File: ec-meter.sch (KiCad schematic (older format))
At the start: 35 parts, among them P1 Probe, P2 V+, P3 OUT, P4 V-, U1 LM324, U2 LM324

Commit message: Started PCB, did some layout, fix some references
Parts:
- C1, C2, C3: footprint visgence_parts:SM1206POL_VIS -> visgence_parts:SM0603_VIS
- C5: footprint (none) -> visgence_parts:SM1206POL_VIS
- D1, D2: footprint (none) -> visgence_parts:SOD-323
- D3, D4: footprint (none) -> LEDs:LED_0603
- P1, P2, P3, P4: footprint (none) -> visgence_parts:Term3.5-2
- R1, R10, R11, R12, R2, R3, R4, R5, R6, R7, R8, R9: footprint visgence_parts:SM1206_VIS -> visgence_parts:SM0603_VIS
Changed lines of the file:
@@
 F 0 "R4" V 2880 1950 50  0000 C CNN
 F 1 "22k" V 2800 1950 50  0000 C CNN
-F 2 "visgence_parts:SM1206_VIS" V 2730 1950 50  0001 C CNN
+F 2 "visgence_parts:SM0603_VIS" V 2730 1950 50  0001 C CNN
 F 3 "" H 2800 1950 50  0000 C CNN
 	1    2800 1950
@@
 F 0 "R2" V 1680 2200 50  0000 C CNN
 F 1 "22k" V 1600 2200 50  0000 C CNN
-F 2 "visgence_parts:SM1206_VIS" V 1530 2200 50  0001 C CNN
+F 2 "visgence_parts:SM0603_VIS" V 1530 2200 50  0001 C CNN
 F 3 "" H 1600 2200 50  0000 C CNN
 	1    1600 2200
@@
 F 0 "R1" V 1430 2200 50  0000 C CNN
 F 1 "10k" V 1350 2200 50  0000 C CNN
-F 2 "visgence_parts:SM1206_VIS" V 1280 2200 50  0001 C CNN
+F 2 "visgence_parts:SM0603_VIS" V 1280 2200 50  0001 C CNN
 F 3 "" H 1350 2200 50  0000 C CNN
 	1    1350 2200
@@
 F 0 "C2" H 2025 2500 50  0000 L CNN
 F 1 "33nF" H 2025 2300 50  0000 L CNN
-F 2 "visgence_parts:SM1206POL_VIS" H 2038 2250 50  0001 C CNN
+F 2 "visgence_parts:SM0603_VIS" H 2038 2250 50  0001 C CNN
 F 3 "" H 2000 2400 50  0000 C CNN
 	1    2000 2400
@@
 F 0 "C1" H 1075 2000 50  0000 L CNN
 F 1 "33nF" H 1075 1800 50  0000 L CNN
-F 2 "visgence_parts:SM1206POL_VIS" H 1088 1750 50  0001 C CNN
+F 2 "visgence_parts:SM0603_VIS" H 1088 1750 50  0001 C CNN
 F 3 "" H 1050 1900 50  0000 C CNN
 	1    1050 1900
@@
 F 0 "R3" V 2880 1250 50  0000 C CNN
 F 1 "22k" V 2800 1250 50  0000 C CNN
-F 2 "visgence_parts:SM1206_VIS" V 2730 1250 50  0001 C CNN
+F 2 "visgence_parts:SM0603_VIS" V 2730 1250 50  0001 C CNN
 F 3 "" H 2800 1250 50  0000 C CNN
 	1    2800 1250
@@
 F 0 "C3" H 3525 2500 50  0000 L CNN
 F 1 "33nF" H 3525 2300 50  0000 L CNN
-F 2 "visgence_parts:SM1206POL_VIS" H 3538 2250 50  0001 C CNN
+F 2 "visgence_parts:SM0603_VIS" H 3538 2250 50  0001 C CNN
 F 3 "" H 3500 2400 50  0000 C CNN
 	1    3500 2400
@@
 F 0 "R8" V 4380 1850 50  0000 C CNN
 F 1 "100k" V 4300 1850 50  0000 C CNN
-F 2 "visgence_parts:SM1206_VIS" V 4230 1850 50  0001 C CNN
+F 2 "visgence_parts:SM0603_VIS" V 4230 1850 50  0001 C CNN
 F 3 "" H 4300 1850 50  0000 C CNN
 	1    4300 1850
@@
 F 0 "R9" V 4680 2150 50  0000 C CNN
 F 1 "3.3k" V 4600 2150 50  0000 C CNN
-F 2 "visgence_parts:SM1206_VIS" V 4530 2150 50  0001 C CNN
+F 2 "visgence_parts:SM0603_VIS" V 4530 2150 50  0001 C CNN
 F 3 "" H 4600 2150 50  0000 C CNN
 	1    4600 2150
@@
 F 0 "R10" V 5930 1700 50  0000 C CNN
 F 1 "4.7k" V 5850 1700 50  0000 C CNN
-F 2 "visgence_parts:SM1206_VIS" V 5780 1700 50  0001 C CNN
+F 2 "visgence_parts:SM0603_VIS" V 5780 1700 50  0001 C CNN
 F 3 "" H 5850 1700 50  0000 C CNN
 	1    5850 1700
@@
 F 0 "P1" H 7075 4925 50  0000 C CNN
 F 1 "Probe" V 7175 4775 50  0000 C CNN
-F 2 "" H 7075 4775 50  0001 C CNN
+F 2 "visgence_parts:Term3.5-2" H 7075 4775 50  0001 C CNN
 F 3 "" H 7075 4775 50  0000 C CNN
 	1    7075 4775
@@
 F 0 "D1" H 2750 5000 50  0000 C CNN
 F 1 "D" H 2750 4800 50  0000 C CNN
-F 2 "" H 2750 4900 50  0001 C CNN
+F 2 "visgence_parts:SOD-323" H 2750 4900 50  0001 C CNN
 F 3 "" H 2750 4900 50  0000 C CNN
 	1    2750 4900
@@
 F 0 "D2" H 3550 4550 50  0000 C CNN
 F 1 "D" H 3550 4350 50  0000 C CNN
-F 2 "" H 3550 4450 50  0001 C CNN
+F 2 "visgence_parts:SOD-323" H 3550 4450 50  0001 C CNN
 F 3 "" H 3550 4450 50  0000 C CNN
 	1    3550 4450
@@
 F 0 "R5" V 3630 4850 50  0000 C CNN
 F 1 "3.3K" V 3550 4850 50  0000 C CNN
-F 2 "visgence_parts:SM1206_VIS" V 3480 4850 50  0001 C CNN
+F 2 "visgence_parts:SM0603_VIS" V 3480 4850 50  0001 C CNN
 F 3 "" H 3550 4850 50  0000 C CNN
 	1    3550 4850
@@
 F 0 "R7" V 4230 5100 50  0000 C CNN
 F 1 "1k" V 4150 5100 50  0000 C CNN
-F 2 "visgence_parts:SM1206_VIS" V 4080 5100 50  0001 C CNN
+F 2 "visgence_parts:SM0603_VIS" V 4080 5100 50  0001 C CNN
 F 3 "" H 4150 5100 50  0000 C CNN
 	1    4150 5100
@@
 F 0 "P2" H 8250 4225 50  0000 C CNN
 F 1 "V+" V 8350 4075 50  0000 C CNN
-F 2 "" H 8250 4075 50  0001 C CNN
+F 2 "visgence_parts:Term3.5-2" H 8250 4075 50  0001 C CNN
 F 3 "" H 8250 4075 50  0000 C CNN
 	1    8250 4075
@@
 F 0 "P4" H 8450 4225 50  0000 C CNN
 F 1 "V-" V 8550 4075 50  0000 C CNN
-F 2 "" H 8450 4075 50  0001 C CNN
+F 2 "visgence_parts:Term3.5-2" H 8450 4075 50  0001 C CNN
 F 3 "" H 8450 4075 50  0000 C CNN
 	1    8450 4075
@@
 F 0 "P3" H 8350 5700 50  0000 C CNN
 F 1 "OUT" V 8450 5550 50  0000 C CNN
-F 2 "" H 8350 5550 50  0001 C CNN
+F 2 "visgence_parts:Term3.5-2" H 8350 5550 50  0001 C CNN
 F 3 "" H 8350 5550 50  0000 C CNN
 	1    8350 5550
@@
 F 0 "R6" V 3630 5350 50  0000 C CNN
 F 1 "10k" V 3550 5350 50  0000 C CNN
-F 2 "visgence_parts:SM1206_VIS" V 3480 5350 50  0001 C CNN
+F 2 "visgence_parts:SM0603_VIS" V 3480 5350 50  0001 C CNN
 F 3 "" H 3550 5350 50  0000 C CNN
 	1    3550 5350
@@
 F 0 "R11" V 9255 1850 50  0000 C CNN
 F 1 "1k" V 9175 1850 50  0000 C CNN
-F 2 "visgence_parts:SM1206_VIS" V 9105 1850 50  0001 C CNN
+F 2 "visgence_parts:SM0603_VIS" V 9105 1850 50  0001 C CNN
 F 3 "" H 9175 1850 50  0000 C CNN
 	1    9175 1850
@@
 F 0 "D3" H 9175 2325 50  0000 C CNN
 F 1 "NEG" H 9175 2125 50  0000 C CNN
-F 2 "" H 9175 2225 50  0001 C CNN
+F 2 "LEDs:LED_0603" H 9175 2225 50  0001 C CNN
 F 3 "" H 9175 2225 50  0000 C CNN
 	1    9175 2225
@@
 F 0 "R12" V 9955 1850 50  0000 C CNN
 F 1 "1k" V 9875 1850 50  0000 C CNN
-F 2 "visgence_parts:SM1206_VIS" V 9805 1850 50  0001 C CNN
+F 2 "visgence_parts:SM0603_VIS" V 9805 1850 50  0001 C CNN
 F 3 "" H 9875 1850 50  0000 C CNN
 	1    9875 1850
@@
 F 0 "D4" H 9875 2325 50  0000 C CNN
 F 1 "POS" H 9875 2125 50  0000 C CNN
-F 2 "" H 9875 2225 50  0001 C CNN
+F 2 "LEDs:LED_0603" H 9875 2225 50  0001 C CNN
 F 3 "" H 9875 2225 50  0000 C CNN
 	1    9875 2225
@@
 F 0 "C5" H 10175 2225 50  0000 L CNN
 F 1 "10uF" H 10175 2025 50  0000 L CNN
-F 2 "" H 10150 2125 50  0001 C CNN
+F 2 "visgence_parts:SM1206POL_VIS" H 10150 2125 50  0001 C CNN
 F 3 "" H 10150 2125 50  0000 C CNN
 	1    10150 2125

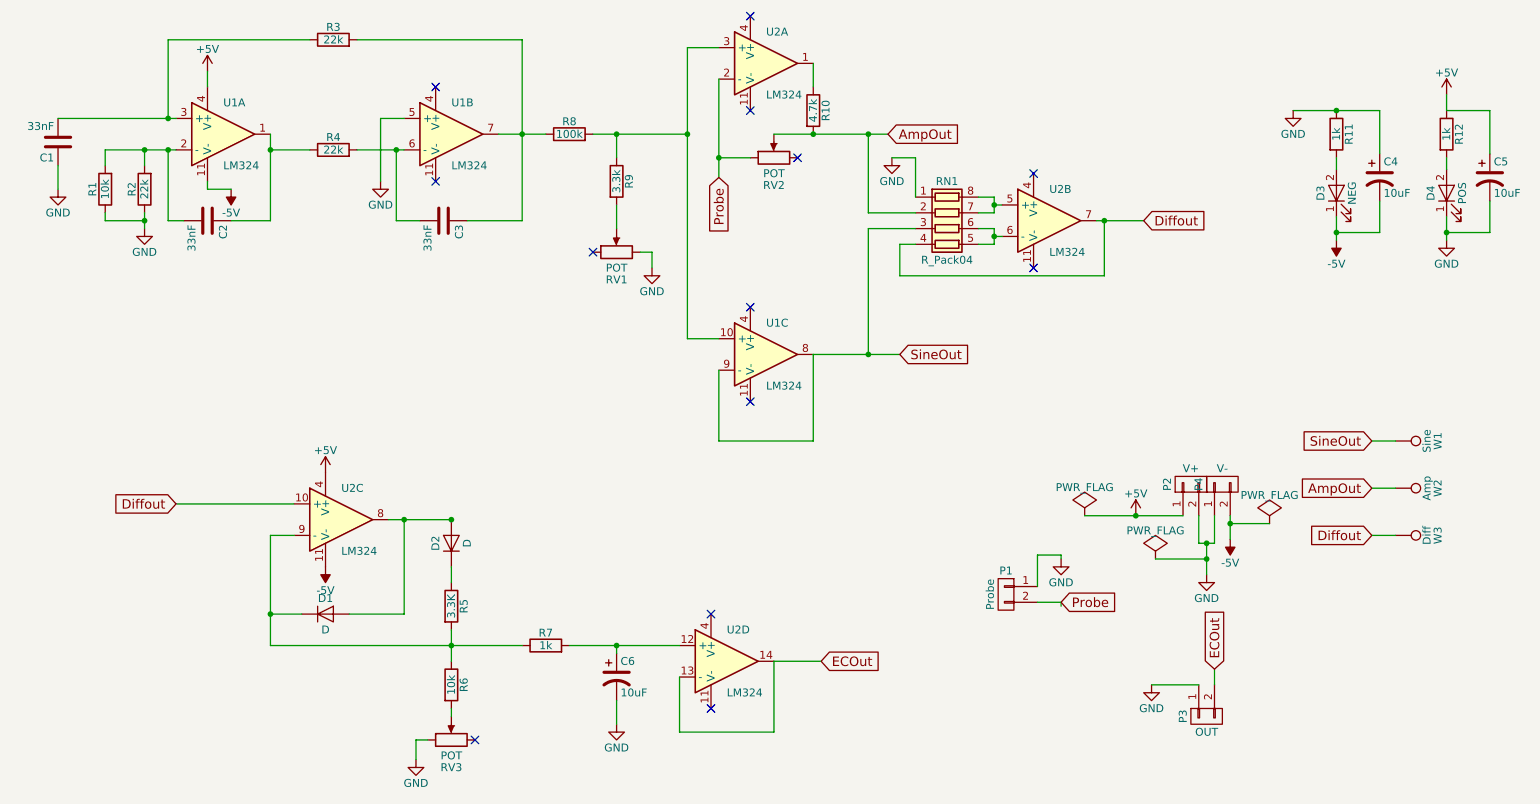
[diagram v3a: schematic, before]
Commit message: Moved parts, rearranged opamps
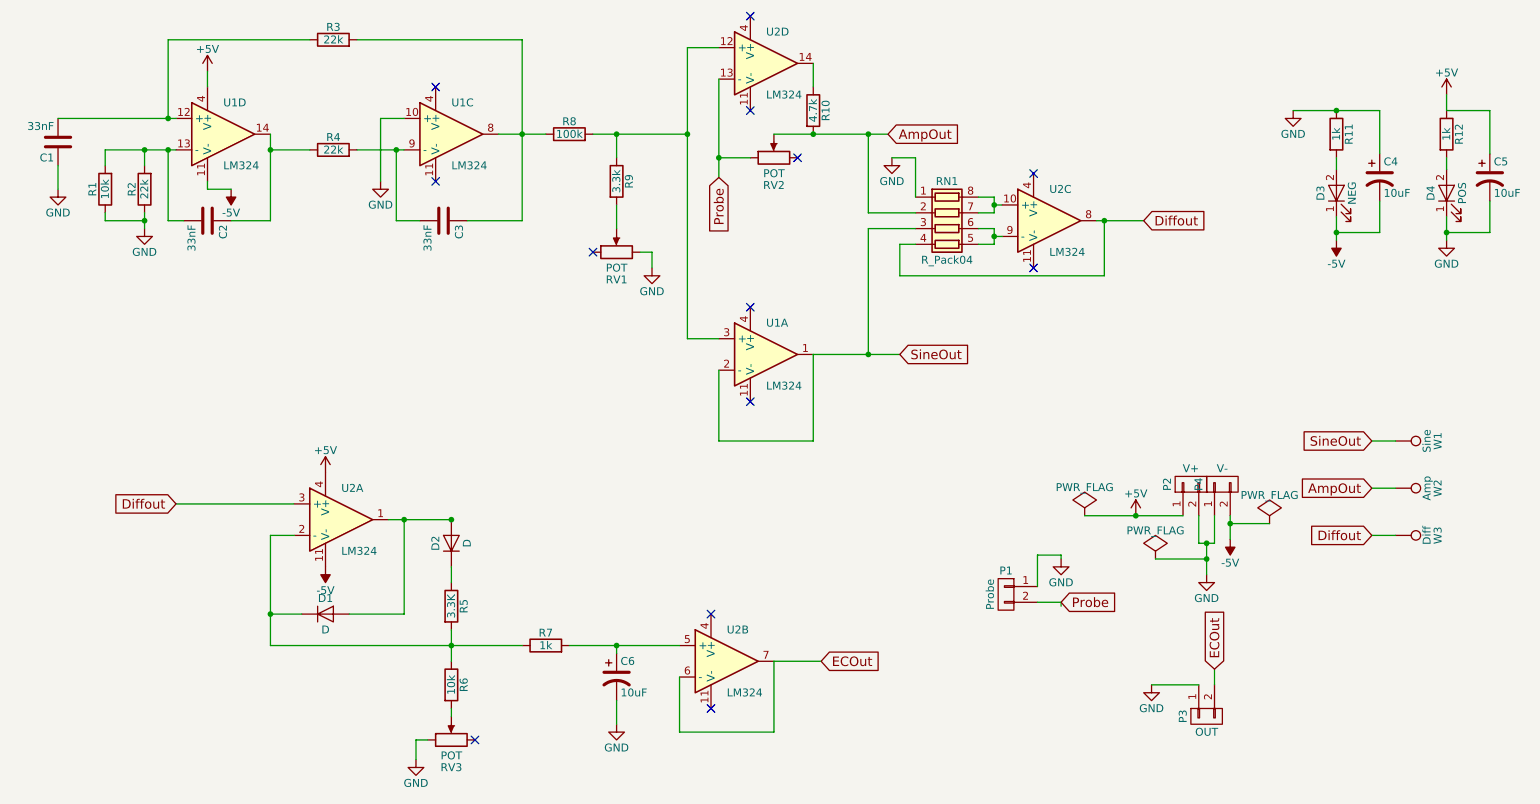
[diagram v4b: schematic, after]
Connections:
- net Diffout: now also U2.3 (+), U2.8; no longer U2.10 (+), U2.7
- net ECOut: now also U2.6 (-), U2.7; no longer U2.13 (-), U2.14
- net GND: now also U1.10 (+); no longer U1.5 (+)
- net Probe: now also U2.13 (-); no longer U2.2 (-)
- net SineOut: now also U1.1, U1.2 (-); no longer U1.8, U1.9 (-)
- net at C2.1, R4.1: now also U1.14; no longer U1.1
- net at C2.2, R1.2, R2.2: now also U1.13 (-); no longer U1.2 (-)
- net at C1.2, R3.1: now also U1.12 (+); no longer U1.3 (+)
- net at C3.2, R4.2: now also U1.9 (-); no longer U1.6 (-)
- net at C3.1, R3.2, R8.1: now also U1.8; no longer U1.7
- net at R8.2, R9.1: now also U1.3 (+), U2.12 (+); no longer U1.10 (+), U2.3 (+)
- net at R10.1: now also U2.14; no longer U2.1
- net at RN1.7 (R2.2), RN1.8 (R1.2): now also U2.10 (+); no longer U2.5 (+)
- net at RN1.5 (R4.2), RN1.6 (R3.2): now also U2.9 (-); no longer U2.6 (-)
- net at D1.2 (A), D2.2 (A): now also U2.1; no longer U2.8
- net at D1.1 (K), R5.2, R6.1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: now also U2.2 (-); no longer U2.9 (-)
- net at C6.1, R7.2: now also U2.5 (+); no longer U2.12 (+)
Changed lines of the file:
@@
 $Comp
 L LM324 U1
-U 1 1 58825C06
+U 4 1 58825C06
 P 2100 1850
 F 0 "U1" H 2100 2050 50  0000 L CNN
@@
 F 2 "SMD_Packages:SOIC-14_N" H 2050 1950 50  0001 C CNN
 F 3 "" H 2150 2050 50  0000 C CNN
-	1    2100 1850
+	4    2100 1850
 	1    0    0    -1
 $EndComp
 $Comp
 L LM324 U1
-U 2 1 58825C58
+U 3 1 58825C58
 P 3550 1850
 F 0 "U1" H 3550 2050 50  0000 L CNN
@@
 F 2 "SMD_Packages:SOIC-14_N" H 3500 1950 50  0001 C CNN
 F 3 "" H 3600 2050 50  0000 C CNN
-	2    3550 1850
+	3    3550 1850
 	1    0    0    -1
 $EndComp
@@
 $Comp
 L LM324 U2
-U 1 1 588284D0
+U 4 1 588284D0
 P 5550 1400
 F 0 "U2" H 5550 1600 50  0000 L CNN
@@
 F 2 "SMD_Packages:SOIC-14_N" H 5500 1500 50  0001 C CNN
 F 3 "" H 5600 1600 50  0000 C CNN
-	1    5550 1400
+	4    5550 1400
 	1    0    0    -1
 $EndComp
 $Comp
 L LM324 U2
-U 2 1 5882852F
+U 3 1 5882852F
 P 7350 2400
 F 0 "U2" H 7350 2600 50  0000 L CNN
@@
 F 2 "SMD_Packages:SOIC-14_N" H 7300 2500 50  0001 C CNN
 F 3 "" H 7400 2600 50  0000 C CNN
-	2    7350 2400
+	3    7350 2400
 	1    0    0    -1
 $EndComp
 $Comp
 L LM324 U2
-U 3 1 58828578
+U 1 1 58828578
 P 2850 4300
 F 0 "U2" H 2850 4500 50  0000 L CNN
@@
 F 2 "SMD_Packages:SOIC-14_N" H 2800 4400 50  0001 C CNN
 F 3 "" H 2900 4500 50  0000 C CNN
-	3    2850 4300
+	1    2850 4300
 	1    0    0    -1
 $EndComp
 $Comp
 L LM324 U2
-U 4 1 588285F1
+U 2 1 588285F1
 P 5300 5200
 F 0 "U2" H 5300 5400 50  0000 L CNN
@@
 F 2 "SMD_Packages:SOIC-14_N" H 5250 5300 50  0001 C CNN
 F 3 "" H 5350 5400 50  0000 C CNN
-	4    5300 5200
+	2    5300 5200
 	1    0    0    -1
 $EndComp
@@
 $Comp
 L LM324 U1
-U 3 1 5883D424
+U 1 1 5883D424
 P 5550 3250
 F 0 "U1" H 5550 3450 50  0000 L CNN
@@
 F 2 "SMD_Packages:SOIC-14_N" H 5500 3350 50  0001 C CNN
 F 3 "" H 5600 3450 50  0000 C CNN
-	3    5550 3250
-	1    0    0    -1
-$EndComp
+	1    5550 3250
+	1    0    0    -1
+$EndComp

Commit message: Did routing
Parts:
- C1, C2, C3: footprint visgence_parts:SM0603_VIS -> visgence_parts:SM1206_VIS
- D1, D2: footprint visgence_parts:SOD-323 -> Diodes_SMD:D_SOD-323_HandSoldering
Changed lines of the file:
@@
 F 0 "C2" H 2025 2500 50  0000 L CNN
 F 1 "33nF" H 2025 2300 50  0000 L CNN
-F 2 "visgence_parts:SM0603_VIS" H 2038 2250 50  0001 C CNN
+F 2 "visgence_parts:SM1206_VIS" H 2038 2250 50  0001 C CNN
 F 3 "" H 2000 2400 50  0000 C CNN
 	1    2000 2400
@@
 F 0 "C1" H 1075 2000 50  0000 L CNN
 F 1 "33nF" H 1075 1800 50  0000 L CNN
-F 2 "visgence_parts:SM0603_VIS" H 1088 1750 50  0001 C CNN
+F 2 "visgence_parts:SM1206_VIS" H 1088 1750 50  0001 C CNN
 F 3 "" H 1050 1900 50  0000 C CNN
 	1    1050 1900
@@
 F 0 "C3" H 3525 2500 50  0000 L CNN
 F 1 "33nF" H 3525 2300 50  0000 L CNN
-F 2 "visgence_parts:SM0603_VIS" H 3538 2250 50  0001 C CNN
+F 2 "visgence_parts:SM1206_VIS" H 3538 2250 50  0001 C CNN
 F 3 "" H 3500 2400 50  0000 C CNN
 	1    3500 2400
@@
 F 0 "D1" H 2750 5000 50  0000 C CNN
 F 1 "D" H 2750 4800 50  0000 C CNN
-F 2 "visgence_parts:SOD-323" H 2750 4900 50  0001 C CNN
+F 2 "Diodes_SMD:D_SOD-323_HandSoldering" H 2750 4900 50  0001 C CNN
 F 3 "" H 2750 4900 50  0000 C CNN
 	1    2750 4900
@@
 F 0 "D2" H 3550 4550 50  0000 C CNN
 F 1 "D" H 3550 4350 50  0000 C CNN
-F 2 "visgence_parts:SOD-323" H 3550 4450 50  0001 C CNN
+F 2 "Diodes_SMD:D_SOD-323_HandSoldering" H 3550 4450 50  0001 C CNN
 F 3 "" H 3550 4450 50  0000 C CNN
 	1    3550 4450

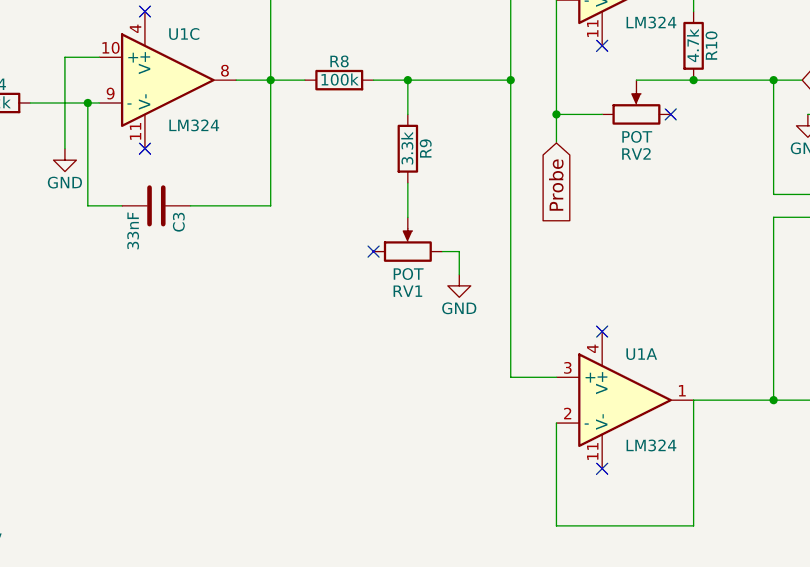
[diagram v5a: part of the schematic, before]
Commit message: Changed direction of RV1
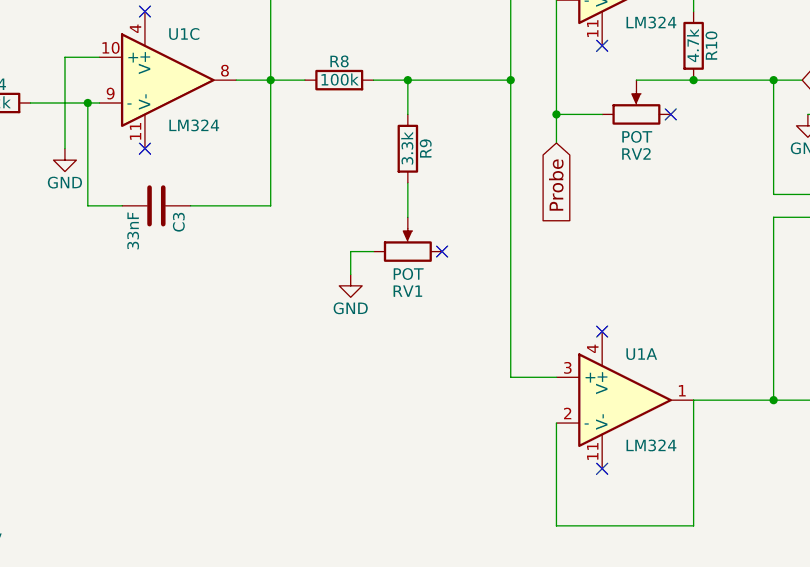
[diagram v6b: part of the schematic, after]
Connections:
- net GND: now also RV1.1; no longer RV1.3
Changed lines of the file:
@@
 L GND #PWR013
 U 1 1 58861427
-P 4825 2700
-F 0 "#PWR013" H 4825 2450 50  0001 C CNN
-F 1 "GND" H 4825 2550 50  0000 C CNN
-F 2 "" H 4825 2700 50  0000 C CNN
-F 3 "" H 4825 2700 50  0000 C CNN
-	1    4825 2700
-	1    0    0    -1
-$EndComp
-Wire Wire Line
-	4825 2600 4825 2700
-Wire Wire Line
-	4825 2600 4750 2600
+P 4350 2700
+F 0 "#PWR013" H 4350 2450 50  0001 C CNN
+F 1 "GND" H 4350 2550 50  0000 C CNN
+F 2 "" H 4350 2700 50  0000 C CNN
+F 3 "" H 4350 2700 50  0000 C CNN
+	1    4350 2700
+	1    0    0    -1
+$EndComp
 $Comp
 L -5V #PWR18
@@
 	8000 5350 8300 5350
 NoConn ~ 3700 5700
-NoConn ~ 4450 2600
 NoConn ~ 5750 2000
 NoConn ~ 3450 1550
@@
 	8350 4450 8350 4650
 Connection ~ 8350 4550
+Wire Wire Line
+	4350 2700 4350 2600
+Wire Wire Line
+	4350 2600 4450 2600
+NoConn ~ 4750 2600
 $EndSCHEMATC

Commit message: Changed diode to reflowable one
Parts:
- D1, D2: footprint Diodes_SMD:D_SOD-323_HandSoldering -> Diodes_SMD:D_SOD-323
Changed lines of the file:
@@
 F 0 "D1" H 2750 5000 50  0000 C CNN
 F 1 "D" H 2750 4800 50  0000 C CNN
-F 2 "Diodes_SMD:D_SOD-323_HandSoldering" H 2750 4900 50  0001 C CNN
+F 2 "Diodes_SMD:D_SOD-323" H 2750 4900 50  0001 C CNN
 F 3 "" H 2750 4900 50  0000 C CNN
 	1    2750 4900
@@
 F 0 "D2" H 3550 4550 50  0000 C CNN
 F 1 "D" H 3550 4350 50  0000 C CNN
-F 2 "Diodes_SMD:D_SOD-323_HandSoldering" H 3550 4450 50  0001 C CNN
+F 2 "Diodes_SMD:D_SOD-323" H 3550 4450 50  0001 C CNN
 F 3 "" H 3550 4450 50  0000 C CNN
 	1    3550 4450
